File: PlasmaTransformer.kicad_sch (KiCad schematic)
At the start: 51 parts, among them J1 Barrel_Jack_MountingPin, J10 Screw_Terminal_01x01, J11 Screw_Terminal_01x01, J12 Screw_Terminal_01x01, J2 Conn_01x02_Pin, J3 Conn_Coaxial, J4 Conn_02x04_Odd_Even, J5 Conn_Coaxial, J6 Screw_Terminal_01x01, J7 Screw_Terminal_01x01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

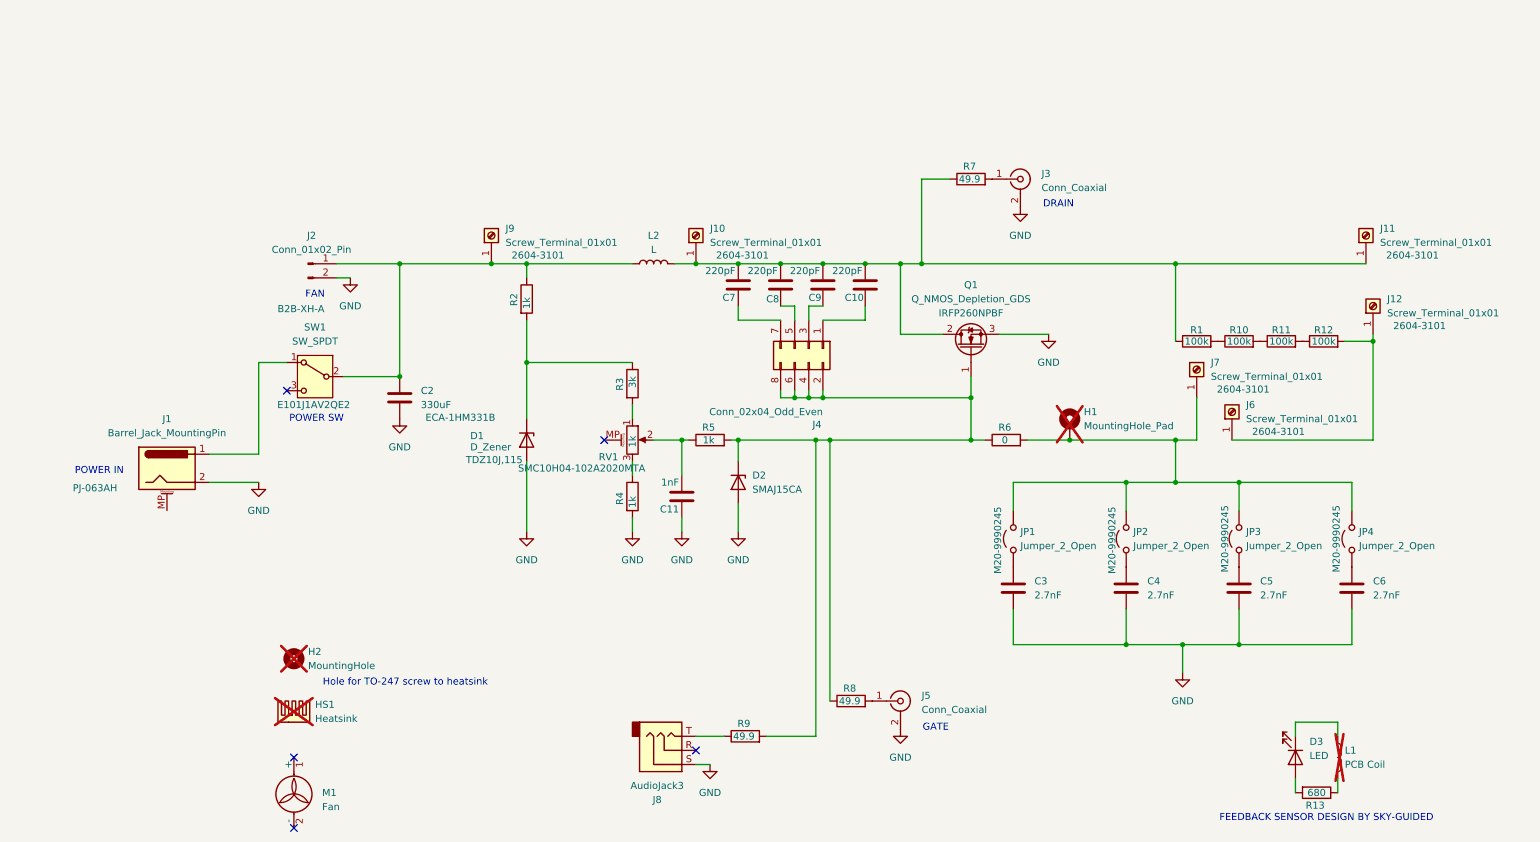
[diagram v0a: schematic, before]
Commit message: modifying recommended values for successful 20cm toroid halo
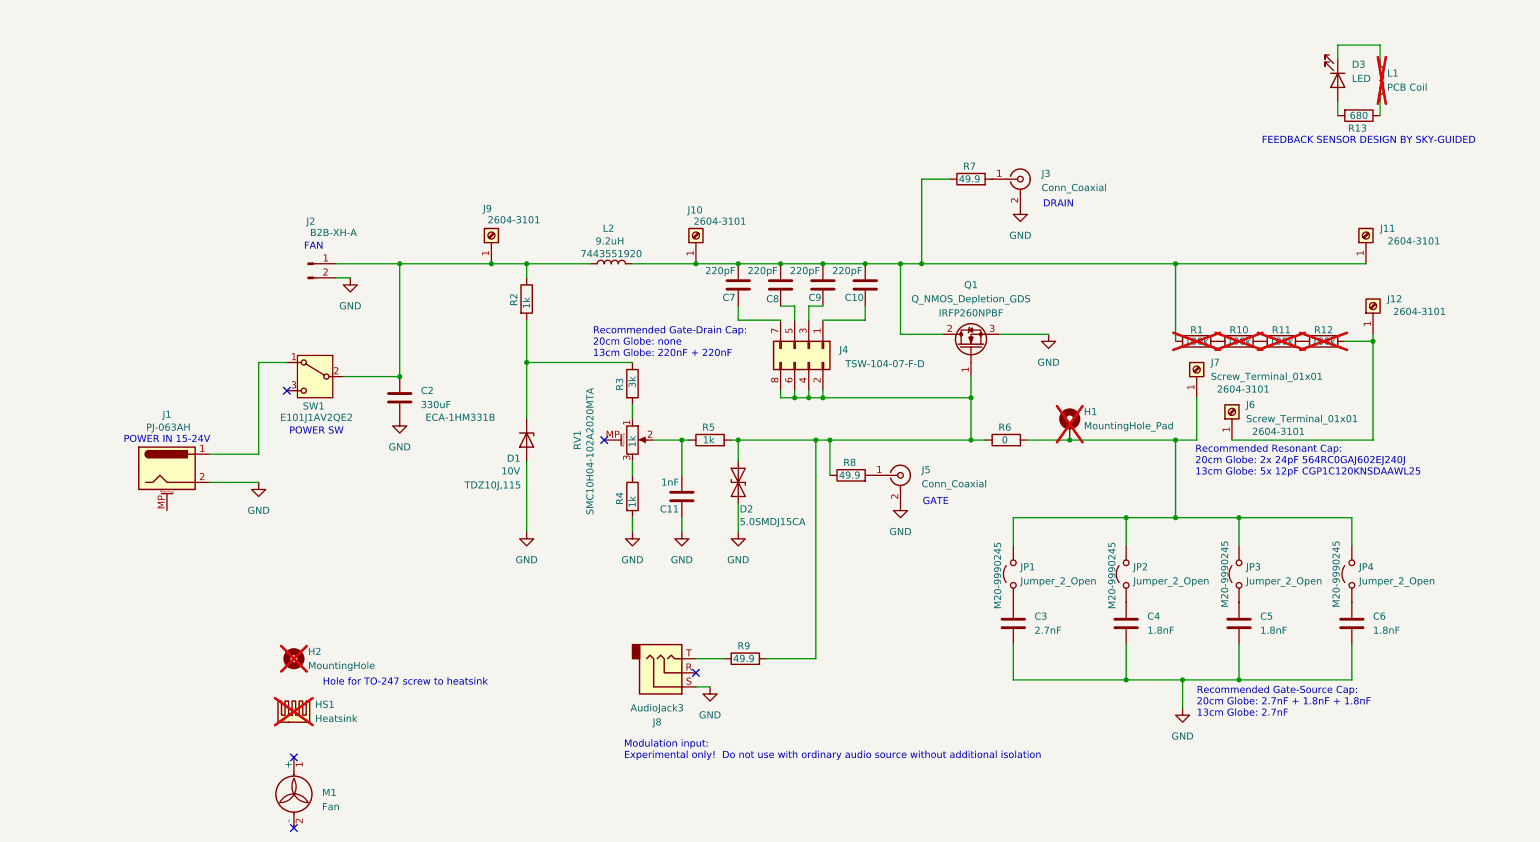
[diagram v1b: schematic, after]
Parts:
- C4, C5, C6: value 2.7nF -> 1.8nF; MPN 1812GC272KAT1A -> C1812C182JCGACTU; Manufacturer Kyocera -> Kemet
- D1: value D_Zener -> 10V
- D2: value SMAJ15CA -> 5.0SMDJ15CA; footprint Diode_SMD:D_SMC -> Diode_SMD:D_SMA; symbol Device:D_Zener -> Diode:SMAJ15CA; MPN SMCJ15A -> 5.0SMDJ15CA
- L2: value L -> 9.2uH; MPN SRP1265C-6R8M -> 7443551920; Manufacturer Bourns -> Wurth
- R1, R10, R11, R12: now not fitted
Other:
- note added: "Modulation input: Experimental only! Do not use with ordinary audio source without additional isolation"
- note added: "POWER IN 15-24V"
- note added: "Recommended Gate-Drain Cap: 20cm Globe: none 13cm Globe: 220nF + 220nF"
- note added: "Recommended Gate-Source Cap: 20cm Globe: 2.7nF + 1.8nF + 1.8nF 13cm Globe: 2.7nF"
- note added: "Recommended Resonant Cap: 20cm Globe: 2x 24pF 564RC0GAJ602EJ240J 13cm Globe: 5x 12pF CGP1C120KNSDAAWL25"
- note removed: "POWER IN"
- moved on the sheet: C3, C4, C5, C6, D3, J5, J8, JP1, JP2, JP3, JP4, L1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

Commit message: rev 3 PCB adds auto ignite
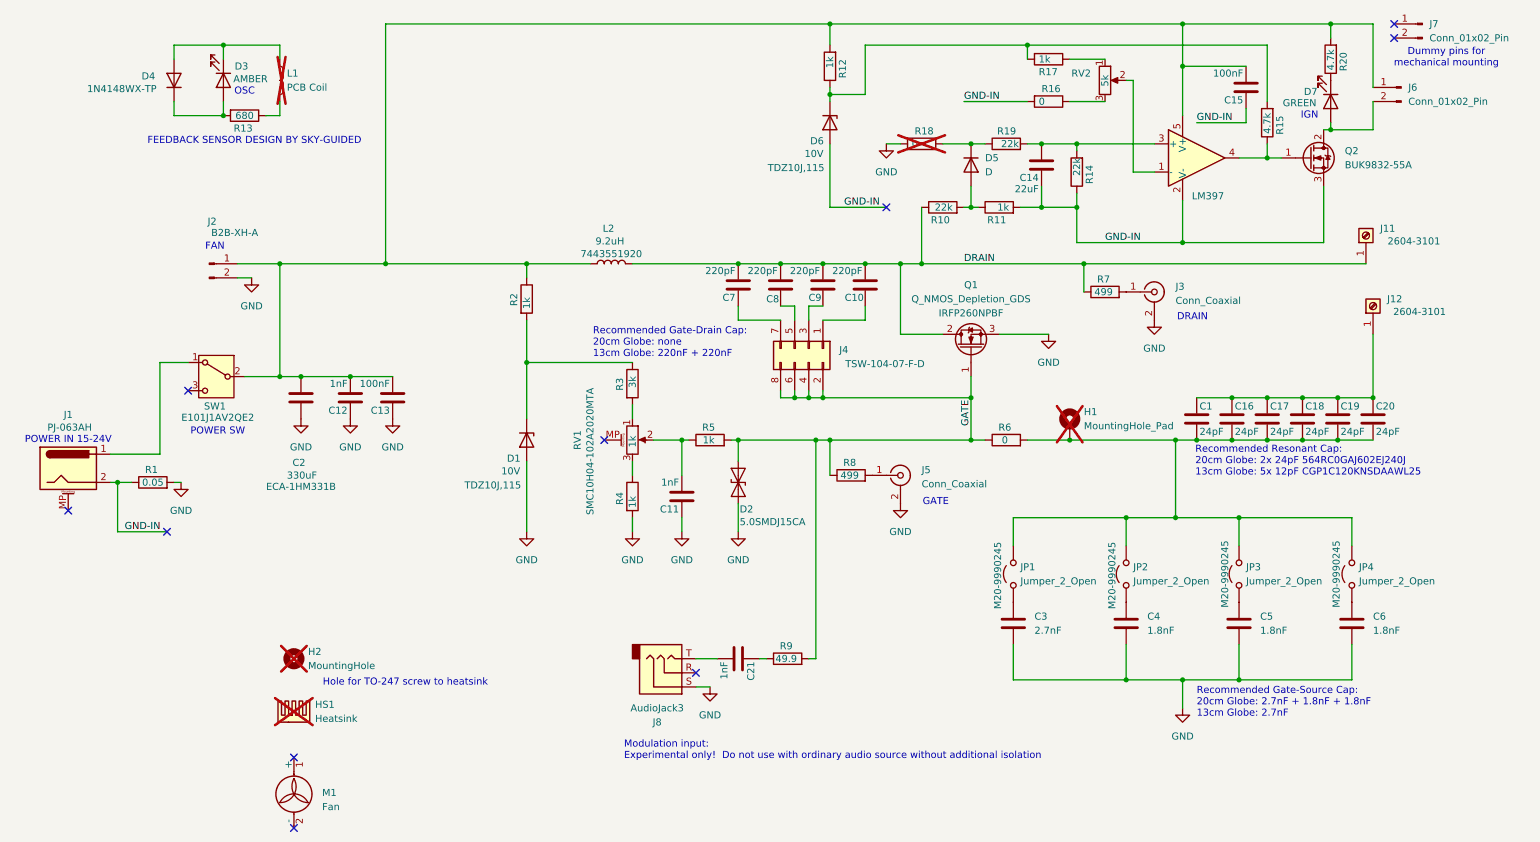
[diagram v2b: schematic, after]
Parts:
- removed J10, J6, J7, J9: Screw_Terminal_01x01, Library:CONN_2604-3101_WAG, symbol Connector:Screw_Terminal_01x01
- added C1, C16, C17, C18, C19, C20: 24pF, Capacitor_THT:C_Disc_D11.0mm_W5.0mm_P10.00mm, symbol Device:C
- added C12, C21: 1nF, Capacitor_SMD:C_1812_4532Metric, symbol Device:C
- added C13: 100nF, Capacitor_SMD:C_1812_4532Metric, symbol Device:C
- added C14: 22uF, Capacitor_SMD:C_0805_2012Metric, symbol Device:C
- added C15: 100nF, Capacitor_SMD:C_0805_2012Metric, symbol Device:C
- added D4, D5: D, Diode_SMD:D_SOD-323, symbol Device:D
- added D6: 10V, Diode_SMD:D_SOD-323_HandSoldering, symbol Device:D_Zener
- added D7: GREEN, LED_SMD:LED_1206_3216Metric, symbol Device:LED
- added J6, J7: Conn_01x02_Pin, Connector_PinHeader_2.54mm:PinHeader_1x02_P2.54mm_Vertical, symbol Connector:Conn_01x02_Pin
- added Q2: BUK9832-55A, Package_TO_SOT_SMD:SOT-223-3_TabPin2, symbol Transistor_FET:BUK9832-55A
- added R14, R19: 22k, Resistor_SMD:R_0805_2012Metric, symbol Device:R
- added R15, R20: 4.7k, Resistor_SMD:R_0805_2012Metric, symbol Device:R
- added R16, R18: 0, Resistor_SMD:R_0805_2012Metric, symbol Device:R
- added R17: 1k, Resistor_SMD:R_0805_2012Metric, symbol Device:R
- added RV2: 5k, Potentiometer_SMD:Potentiometer_Vishay_TS53YL_Vertical, symbol Device:R_Potentiometer
- added U1: LM397, Package_TO_SOT_SMD:SOT-23-5, symbol Comparator:LM397
- D2: footprint Diode_SMD:D_SMA -> Diode_SMD:D_SMC
- D3: value LED -> AMBER
- R1: value 100k -> 0.05; footprint Resistor_SMD:R_1812_4532Metric -> Resistor_SMD:R_2512_6332Metric; MPN ERJ-12NF1003U -> (none); Manufacturer Panasonic -> (none); now fitted
- R10: value 100k -> 22k; footprint Resistor_SMD:R_1812_4532Metric -> Resistor_SMD:R_0805_2012Metric; MPN ERJ-12NF1003U -> (none); Manufacturer Panasonic -> (none); now fitted
- R11, R12: value 100k -> 1k; footprint Resistor_SMD:R_1812_4532Metric -> Resistor_SMD:R_0805_2012Metric; MPN ERJ-12NF1003U -> RC0805FR-071KL; Manufacturer Panasonic -> Yageo; now fitted
- R7, R8: value 49.9 -> 499; footprint Resistor_SMD:R_0805_2012Metric -> Resistor_SMD:R_2010_5025Metric; MPN RC0805FR-0749R9L -> RC2010FK-07499RL
- R9: footprint Resistor_SMD:R_0805_2012Metric -> Resistor_SMD:R_2010_5025Metric; MPN RC0805FR-0749R9L -> RC2010FK-0749R9L
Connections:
- net GND: now also R1.2, C12.1, C13.1, R18.2; no longer J1.2
- net GATE: now reaches D2.1 (A1), J4.2 (Pin_2), J4.4 (Pin_4), J4.6 (Pin_6), J4.8 (Pin_8), Q1.1 (G), R5.2, R6.1, R8.1, R9.2
- net at R12.1: now also D6.1 (K), R15.2, R17.2; no longer R11.2
- net at R12.2: now also C2.1, J2.1 (Pin_1), L2.1, R2.1, SW1.2 (B), C12.2, C13.2, C15.2, J6.1 (Pin_1), R20.2, U1.5 (V+); no longer J12.1 (Pin_1)
- net at H1.1, JP1.2 (B), JP2.2 (B)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: now also C1.2, C16.2, C17.2, C18.2, C19.2, C20.2
- net DRAIN: now reaches C10.2, C7.2, C8.2, C9.2, J11.1 (Pin_1), L2.2, Q1.2 (D), R7.1
- net DRAIN: now also R10.1; no longer R1.1
- net at R9.1: now also C21.1; no longer J8.T
- net at R10.2, R11.1: now also D5.2 (A)
- net at D3.1 (K), L1.1: now also D4.2 (A)
- net at D3.2 (A), R13.2: now also D4.1 (K)
- new net: D7.1 (K), R20.1
- new net: R17.1, RV2.1
- new net: RV2.2, U1.1 (-)
- new net: R16.1, RV2.3
- new net: D5.1 (K), R18.1, R19.1
- new net: C14.2, R14.2, R19.2, U1.3 (+)
- new net: C21.2, J8.T
- new net: Q2.1 (G), R15.1, U1.4
- new net: D7.2 (A), J6.2 (Pin_2), Q2.2 (D)
- new net: C1.1, C16.1, C17.1, C18.1, C19.1, C20.1, J12.1 (Pin_1)
- new net GND-IN: C14.1, C15.1, D6.2 (A), J1.2, Q2.3 (S), R1.1, R11.2, R14.1, R16.2, U1.2 (V-)
- no-connect marks 5 -> 10
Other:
- note added: "Dummy pins for mechanical mounting"
- note added: "IGN"
- note added: "OSC"
- moved on the sheet: C2, D3, J1, J2, J3, L1, R13, R7, R9, SW1

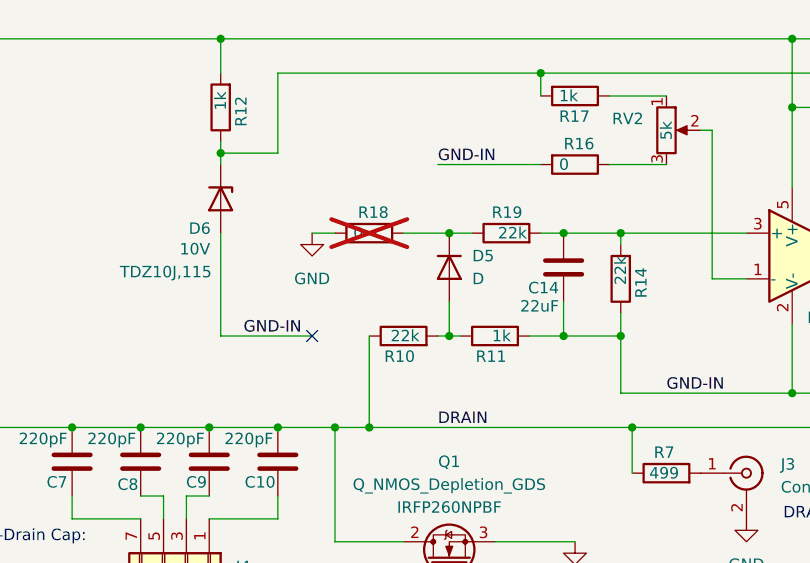
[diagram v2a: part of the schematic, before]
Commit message: Design cleanup, part selection and BOM update
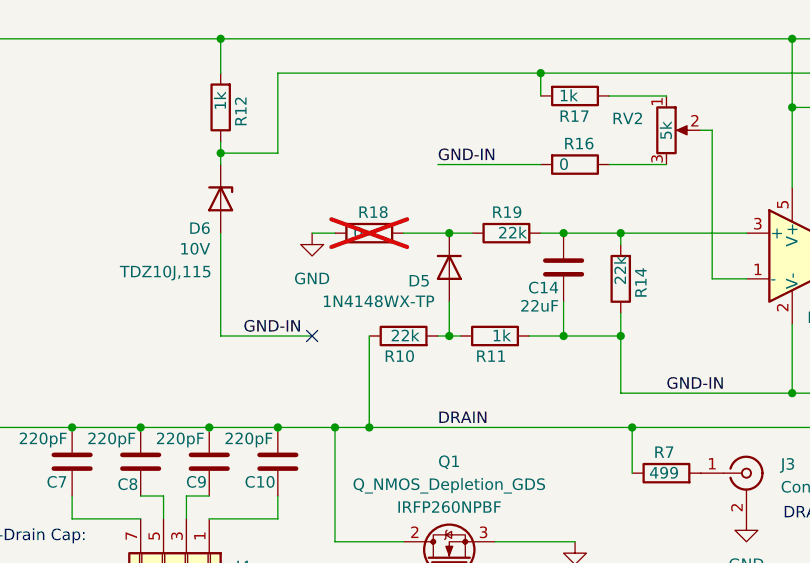
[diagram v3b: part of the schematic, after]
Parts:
- C13: MPN (none) -> GRM43DR7LW104KW01K; Manufacturer (none) -> Murata
- C14: MPN (none) -> GRM21BR61E226ME44L; Manufacturer (none) -> Murata
- C15: MPN (none) -> CL21B104KCFNNNE; Manufacturer (none) -> Samsung
- J6, J7: MPN (none) -> ESQ-102-33-G-S; Manufacturer (none) -> Samtec
- Q2: MPN (none) -> BUK9832-55A/CUX; Manufacturer (none) -> Nexperia
- R1: MPN (none) -> CRA2512-FZ-R050ELF; Manufacturer (none) -> Bourns
- R10, R14, R19: MPN (none) -> RC0805FR-1322KL; Manufacturer (none) -> Yageo
- R15, R20: MPN (none) -> RC0805FR-134K7L
- R16, R18: MPN (none) -> RC0805JR-070RL; Manufacturer (none) -> Yageo
- U1: MPN (none) -> LM397MF/NOPB; Manufacturer (none) -> TI
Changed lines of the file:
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@@
 			)
 		)
-		(property "MPN" ""
+		(property "MPN" "RC0805FR-134K7L"
 			(at 250.19 22.86 90)
 			(effects
@@
 			)
 		)
+		(property "MPN" "CRA2512-FZ-R050ELF"
+			(at 38.1 99.06 90)
+			(effects
+				(font
+					(size 1.27 1.27)
+				)
+				(hide yes)
+			)
+		)
+		(property "Manufacturer" "Bourns"
+			(at 38.1 99.06 90)
+			(effects
+				(font
+					(size 1.27 1.27)
+				)
+				(hide yes)
+			)
+		)
 		(pin "1"
 		)
@@
 			)
 		)
-		(property "MPN" ""
+		(property "MPN" "RC0805FR-1322KL"
 			(at 191.77 38.1 90)
 			(effects
@@
 			)
 		)
-		(property "Manufacturer" ""
+		(property "Manufacturer" "Yageo"
 			(at 191.77 38.1 90)
 			(effects
@@
 			)
 		)
+		(property "MPN" "ESQ-102-33-G-S"
+			(at 266.7 16.51 0)
+			(effects
+				(font
+					(size 1.27 1.27)
+				)
+				(hide yes)
+			)
+		)
+		(property "Manufacturer" "Samtec"
+			(at 266.7 16.51 0)
+			(effects
+				(font
+					(size 1.27 1.27)
+				)
+				(hide yes)
+			)
+		)
 		(pin "2"
 		)
@@
 			)
 		)
-		(property "MPN" ""
+		(property "MPN" "RC0805FR-134K7L"
 			(at 238.76 34.29 90)
 			(effects
@@
 			)
 		)
+		(property "MPN" "LM397MF/NOPB"
+			(at 226.06 40.64 0)
+			(effects
+				(font
+					(size 1.27 1.27)
+				)
+				(hide yes)
+			)
+		)
+		(property "Manufacturer" "TI"
+			(at 226.06 40.64 0)
+			(effects
+				(font
+					(size 1.27 1.27)
+				)
+				(hide yes)
+			)
+		)
 		(pin "2"
 		)
@@
 			)
 		)
+		(property "MPN" "BUK9832-55A/CUX"
+			(at 246.38 40.64 0)
+			(effects
+				(font
+					(size 1.27 1.27)
+				)
+				(hide yes)
+			)
+		)
+		(property "Manufacturer" "Nexperia"
+			(at 246.38 40.64 0)
+			(effects
+				(font
+					(size 1.27 1.27)
+				)
+				(hide yes)
+			)
+		)
 		(pin "1"
 		)
@@
 			)
 		)
-		(property "MPN" ""
+		(property "MPN" "RC0805JR-070RL"
 			(at 176.53 38.1 90)
 			(effects
@@
 			)
 		)
-		(property "Manufacturer" ""
+		(property "Manufacturer" "Yageo"
 			(at 176.53 38.1 90)
 			(effects
@@
 			)
 		)
-		(property "MPN" ""
+		(property "MPN" "RC0805FR-1322KL"
 			(at 180.34 49.53 90)
 			(effects
@@
 			)
 		)
-		(property "Manufacturer" ""
+		(property "Manufacturer" "Yageo"
 			(at 180.34 49.53 90)
 			(effects
@@
 			)
 		)
-		(property "Manufacturer" ""
+		(property "Manufacturer" "Murata"
 			(at 198.12 41.91 0)
 			(effects
@@
 			)
 		)
-		(property "MPN" ""
+		(property "MPN" "GRM21BR61E226ME44L"
 			(at 196.85 33.02 0)
 			(effects
@@
 			)
 		)
-		(property "Manufacturer" ""
+		(property "Manufacturer" "Samsung"
 			(at 234.95 27.94 0)
 			(effects
@@
 			)
 		)
-		(property "MPN" ""
+		(property "MPN" "CL21B104KCFNNNE"
 			(at 233.68 19.05 0)
 			(effects
@@
 		(on_board yes)
 		(dnp no)
-		(fields_autoplaced yes)
 		(property "Reference" "D5"
-			(at 187.96 40.6399 90)
+			(at 180.848 43.434 90)
 			(effects
 				(font
@@
 				)
 				(justify left)
+				(hide yes)
 			)
 		)
@@
 		)
 		(property "MPN" "1N4148WX-TP"
-			(at 185.42 41.91 90)
+			(at 177.546 45.72 90)
 			(effects
 				(font
 					(size 1.27 1.27)
 				)
-				(hide yes)
 			)
 		)
@@
 			)
 		)
-		(property "Manufacturer" ""
+		(property "Manufacturer" "Murata"
 			(at 81.28 83.82 0)
 			(effects
@@
 			)
 		)
-		(property "MPN" ""
+		(property "MPN" "GRM43DR7LW104KW01K"
 			(at 80.01 74.93 0)
 			(effects
@@
 			)
 		)
-		(property "MPN" ""
+		(property "MPN" "RC0805FR-1322KL"
 			(at 204.47 43.18 90)
 			(effects
@@
 			)
 		)
-		(property "Manufacturer" ""
+		(property "Manufacturer" "Yageo"
 			(at 204.47 43.18 90)
 			(effects
@@
 			)
 		)
-		(property "MPN" ""
+		(property "MPN" "RC0805JR-070RL"
 			(at 199.39 30.48 90)
 			(effects
@@
 			)
 		)
-		(property "Manufacturer" ""
+		(property "Manufacturer" "Yageo"
 			(at 199.39 30.48 90)
 			(effects
@@
 			(at 262.89 27.94 0)
 			(effects
+				(font
+					(size 1.27 1.27)
+				)
+				(hide yes)
+			)
+		)
+		(property "MPN" "ESQ-102-33-G-S"
+			(at 262.89 27.94 0)
+			(effects
+				(font
+					(size 1.27 1.27)
+				)
+				(hide yes)
+			)
+		)
+		(property "Manufacturer" "Samtec"
+			(at 262.89 27.94 0)
+			(effects

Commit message: graphical fixes to BOM
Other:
- company: (none) -> E. CHIU | Circuits Performers LLC
- title: (none) -> Plasma Transformer
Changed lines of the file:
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@@
 	(generator_version "9.0")
 	(paper "A4")
+	(title_block
+		(title "Plasma Transformer")
+		(rev "3")
+		(company "E. CHIU | Circuits Performers LLC")
+	)
 	(text "Hole for TO-247 screw to heatsink"
 		(exclude_from_sim no)
